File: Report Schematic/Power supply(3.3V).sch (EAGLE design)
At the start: 12 parts, among them U2 LMV358, U3 LMV324

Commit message: Schematics for manual
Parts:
- removed R10, R13, R15, R17, R19: 33K, adafruit:R-US_M1206
- removed R11, R12, R14, R16, R18: 22K, adafruit:R-US_M1206
- removed U2: LMV358, SparkFun-IC-Amplifiers:LMV358SOIC
- removed U3: LMV324, SparkFun-IC-Amplifiers:LMV324
- added C4, C5: 10uF, SparkFun-Capacitors:10UF-1206-6.3V-20%
- added D1: WHITE, SparkFun-LED:LED-WHITE1206
- added IC1: LM1117-3.3, lm1117:LM1117IMPX-3.3
- added R2: 330, adafruit:R-US_M1206
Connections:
- removed net 11: U2G1.+IN
- removed net 15: U3G1.+IN
- removed net 41: U3G2.+IN
- removed net 44: U3G3.+IN
- removed net 45: U3G4.+IN
- removed net EX1: R12.1, R13.1
- removed net EX6: R16.1, R17.1
- removed net GND: R10.2, R13.2, R15.2, R17.2, R19.2
- removed net N1: R11.2, U2G1.-IN, U2G1.OUT
- removed net N2: R12.2, U3G1.-IN, U3G1.OUT
- removed net N3: R14.2, U3G2.-IN, U3G2.OUT
- removed net N4: R16.2, U3G3.-IN, U3G3.OUT
- removed net N5: R18.2, U3G4.-IN, U3G4.OUT
- removed net PB4: R10.1, R11.1
- removed net PD2: R14.1, R15.1
- removed net PE4: R18.1, R19.1
- new net 3.3V: C4.2, C5.2, D1.C, IC1.GND
- new net N$26: D1.A, R2.2
- new net VBATTERY: C4.1, IC1.IN
- new net VDD: C5.1, IC1.OUT, R2.1
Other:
- note added: "12V supply(Vbat) from pin 29"
- note added: "3.3V regulated supply"
- note removed: "Connected to 1st channel of External ADC"
- note removed: "Connected to 6th channel of External ADC"
- note removed: "Connected to PB4"
- note removed: "Connected to PD2"
- note removed: "Connected to PE4"
- note removed: "Plug and Play Board"
- note removed: "Sharp IR2 ,Pin 15 on Main Board"
- note removed: "Sharp IR3 ,Pin 41 on Main Board"
- note removed: "Sharp IR4 ,Pin 20 on Main Board"
- note removed: "Sharp IR4 ,Pin 44 on Main Board"
- note removed: "Sharp IR5 ,Pin 45 on Main Board"

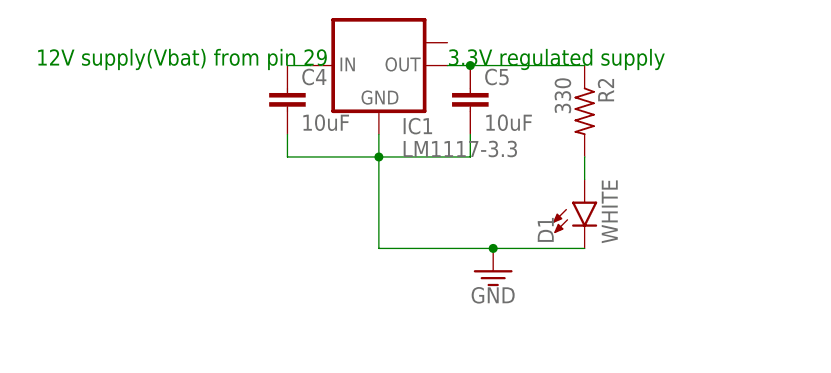
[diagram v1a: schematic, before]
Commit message: Powering and reset switch circuit added to manual
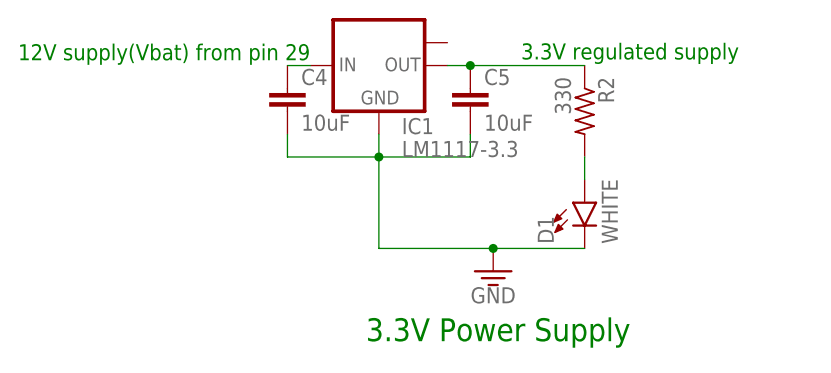
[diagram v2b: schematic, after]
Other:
- note added: "3.3V Power Supply"
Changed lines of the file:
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@@
 <setting verticaltext="up"/>
 </settings>
-<grid distance="0.1" unitdist="inch" unit="inch" style="lines" multiple="1" display="no" altdistance="0.01" altunitdist="inch" altunit="inch"/>
+<grid distance="0.00001" unitdist="inch" unit="inch" style="lines" multiple="1" display="no" altdistance="0.01" altunitdist="inch" altunit="inch"/>
 <layers>
 <layer number="1" name="Top" color="4" fill="1" visible="no" active="no"/>
@@
 <sheet>
 <plain>
-<text x="-27.94" y="38.1" size="1.778" layer="91">12V supply(Vbat) from pin 29</text>
-<text x="17.78" y="38.1" size="1.778" layer="91">3.3V regulated supply</text>
+<text x="-29.93873125" y="38.689790625" size="1.778" layer="91">12V supply(Vbat) from pin 29</text>
+<text x="25.957275" y="38.7786875" size="1.778" layer="91">3.3V regulated supply</text>
+<text x="8.7122" y="7.4747125" size="2.54" layer="91">3.3V Power Supply</text>
 </plain>
 <instances>
